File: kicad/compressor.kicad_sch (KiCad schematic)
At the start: 24 parts, among them J6 Conn_01x06, U8 NE5532, U9 NE5532

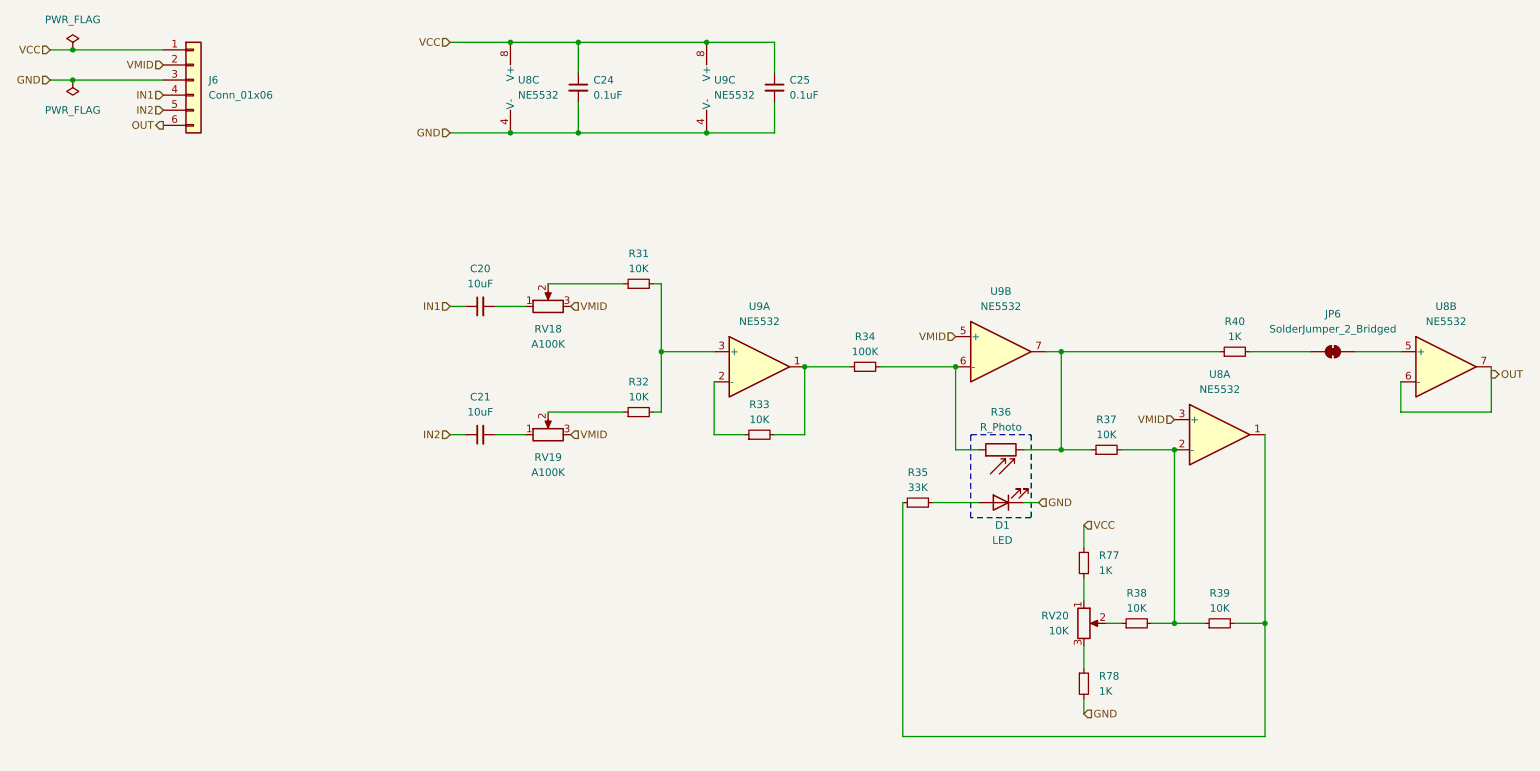
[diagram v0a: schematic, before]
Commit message: fix mixers in filter and compressor, update pcb
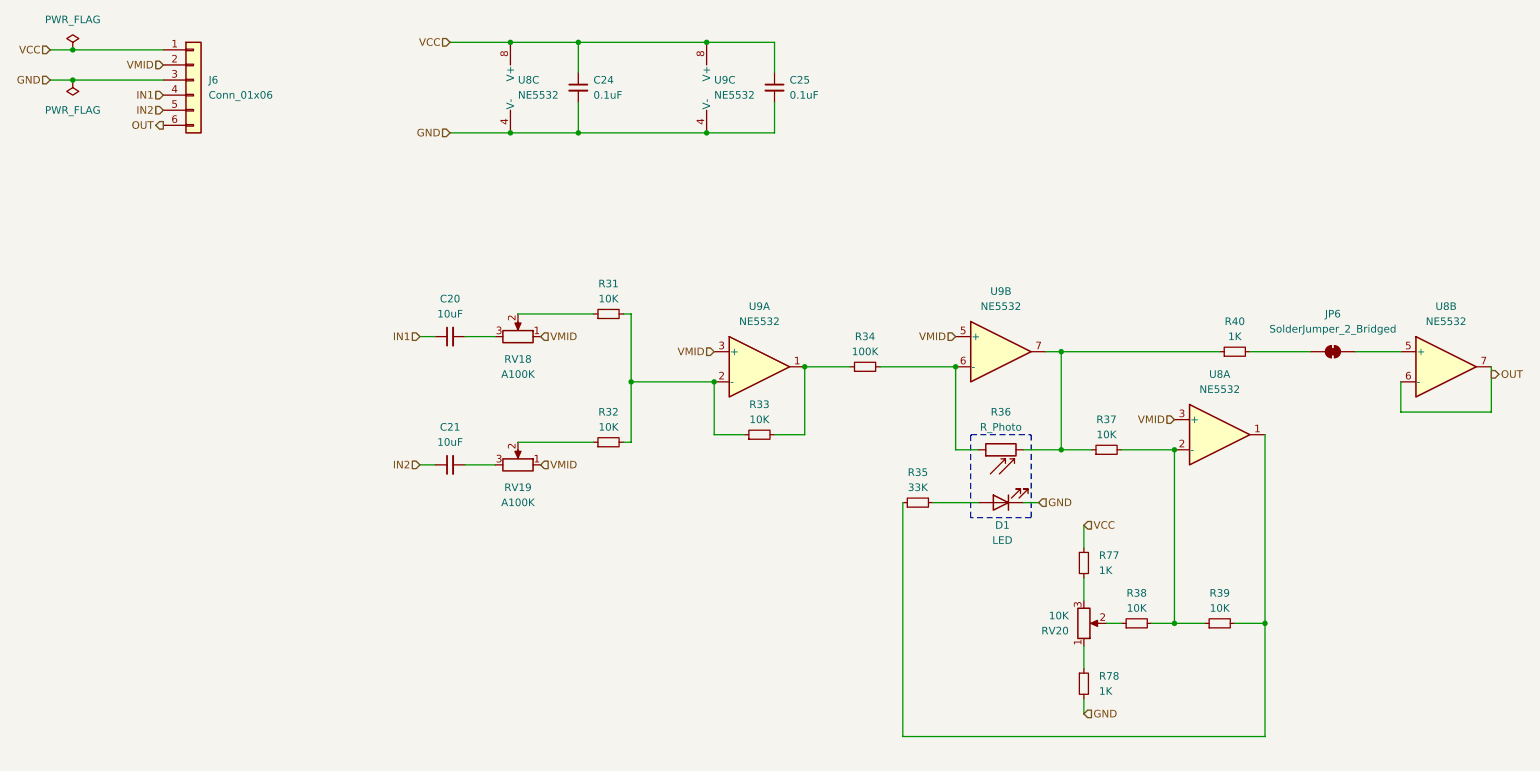
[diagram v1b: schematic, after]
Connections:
- net VMID: now also RV18.1, RV19.1, U9.3 (+); no longer RV18.3, RV19.3
- net at R33.1, U9.2 (-): now also R31.2, R32.2
- net at C21.2: now also RV19.3; no longer RV19.1
- net at R78.1: now also RV20.1; no longer RV20.3
- net at C20.2: now also RV18.3; no longer RV18.1
- net at R77.2: now also RV20.3; no longer RV20.1
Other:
- moved on the sheet: C20, C21, R31, R32, RV18, RV19
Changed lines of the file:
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@@
 	)
 	(junction
-		(at 125.73 88.9)
+		(at 120.65 93.98)
 		(diameter 0)
 		(color 0 0 0 0)
@@
 	)
 	(junction
+		(at 134.62 93.98)
+		(diameter 0)
+		(color 0 0 0 0)
+	)
+	(junction
 		(at 175.26 91.44)
 		(diameter 0)
@@
 	(wire
 		(pts
+			(xy 120.65 93.98) (xy 134.62 93.98)
+		)
+		(stroke
+			(width 0)
+			(type default)
+		)
+	)
+	(wire
+		(pts
 			(xy 111.76 52.07) (xy 133.35 52.07)
 		)
@@
 	(wire
 		(pts
-			(xy 106.68 77.47) (xy 119.38 77.47)
+			(xy 101.6 82.55) (xy 114.3 82.55)
 		)
 		(stroke
@@
 	(wire
 		(pts
-			(xy 97.79 102.87) (xy 102.87 102.87)
-		)
-		(stroke
-			(width 0)
-			(type default)
-		)
-	)
-	(wire
-		(pts
-			(xy 97.79 81.28) (xy 102.87 81.28)
+			(xy 92.71 107.95) (xy 97.79 107.95)
+		)
+		(stroke
+			(width 0)
+			(type default)
+		)
+	)
+	(wire
+		(pts
+			(xy 92.71 86.36) (xy 97.79 86.36)
 		)
 		(stroke
@@
 	(wire
 		(pts
-			(xy 125.73 77.47) (xy 125.73 88.9)
+			(xy 120.65 82.55) (xy 120.65 93.98)
 		)
 		(stroke
@@
 	(wire
 		(pts
+			(xy 120.65 93.98) (xy 120.65 104.14)
+		)
+		(stroke
+			(width 0)
+			(type default)
+		)
+	)
+	(wire
+		(pts
 			(xy 203.2 105.41) (xy 212.09 105.41)
 		)
@@
 	(wire
 		(pts
-			(xy 92.71 102.87) (xy 90.17 102.87)
-		)
-		(stroke
-			(width 0)
-			(type default)
-		)
-	)
-	(wire
-		(pts
-			(xy 125.73 88.9) (xy 125.73 99.06)
+			(xy 87.63 107.95) (xy 85.09 107.95)
 		)
 		(stroke
@@
 	(wire
 		(pts
-			(xy 92.71 81.28) (xy 90.17 81.28)
-		)
-		(stroke
-			(width 0)
-			(type default)
-		)
-	)
-	(wire
-		(pts
-			(xy 125.73 88.9) (xy 134.62 88.9)
+			(xy 87.63 86.36) (xy 85.09 86.36)
 		)
 		(stroke
@@
 	(wire
 		(pts
-			(xy 124.46 77.47) (xy 125.73 77.47)
+			(xy 119.38 82.55) (xy 120.65 82.55)
 		)
 		(stroke
@@
 	(wire
 		(pts
-			(xy 106.68 99.06) (xy 119.38 99.06)
+			(xy 101.6 104.14) (xy 114.3 104.14)
 		)
 		(stroke
@@
 	(wire
 		(pts
-			(xy 124.46 99.06) (xy 125.73 99.06)
+			(xy 119.38 104.14) (xy 120.65 104.14)
 		)
 		(stroke
@@
 		)
 	)
+	(hierarchical_label "VMID"
+		(shape input)
+		(at 134.62 88.9 180)
+		(effects
+			(font
+				(size 1.27 1.27)
+			)
+			(justify right)
+		)
+	)
 	(hierarchical_label "VCC"
 		(shape input)
@@
 	(hierarchical_label "VMID"
 		(shape input)
-		(at 110.49 81.28 0)
+		(at 105.41 86.36 0)
 		(effects
 			(font
@@
 	(hierarchical_label "VMID"
 		(shape input)
-		(at 110.49 102.87 0)
+		(at 105.41 107.95 0)
 		(effects
 			(font
@@
 	(hierarchical_label "IN2"
 		(shape input)
-		(at 90.17 102.87 180)
+		(at 85.09 107.95 180)
 		(effects
 			(font
@@
 	(hierarchical_label "IN1"
 		(shape input)
-		(at 90.17 81.28 180)
+		(at 85.09 86.36 180)
 		(effects
 			(font
@@
 		(on_board yes)
 		(dnp no)
-		(fields_autoplaced yes)
 		(property "Reference" "U9"
 			(at 142.24 81.28 0)
@@
 	(symbol
 		(lib_id "Device:R_Potentiometer")
-		(at 106.68 102.87 90)
+		(at 101.6 107.95 270)
+		(mirror x)
 		(unit 1)
 		(exclude_from_sim no)
@@
 		(on_board yes)
 		(dnp no)
-		(fields_autoplaced yes)
 		(property "Reference" "RV19"
-			(at 106.68 106.68 90)
+			(at 101.6 111.76 90)
 			(effects
 				(font
@@
 		)
 		(property "Value" "A100K"
-			(at 106.68 109.22 90)
+			(at 101.6 114.3 90)
 			(effects
 				(font
@@
 		)
 		(property "Footprint" "Pot_RV09AF-ALPHA:Pot_RV09AF-ALPHA"
-			(at 106.68 102.87 0)
+			(at 101.6 107.95 0)
 			(effects
 				(font
@@
 		)
 		(property "Datasheet" "~"
-			(at 106.68 102.87 0)
+			(at 101.6 107.95 0)
 			(effects
 				(font
@@
 		)
 		(property "Description" "Potentiometer"
-			(at 106.68 102.87 0)
+			(at 101.6 107.95 0)
 			(effects
 				(font
@@
 	(symbol
 		(lib_id "Device:R_Small")
-		(at 121.92 99.06 90)
+		(at 116.84 104.14 90)
 		(unit 1)
 		(exclude_from_sim no)
@@
 		(fields_autoplaced yes)
 		(property "Reference" "R32"
-			(at 121.92 93.98 90)
+			(at 116.84 99.06 90)
 			(effects
 				(font
@@
 		)
 		(property "Value" "10K"
-			(at 121.92 96.52 90)
+			(at 116.84 101.6 90)
 			(effects
 				(font
@@
 		)
 		(property "Footprint" "Resistor_SMD:R_0603_1608Metric"
-			(at 121.92 99.06 0)
+			(at 116.84 104.14 0)
 			(effects
 				(font
@@
 		)
 		(property "Datasheet" "~"
-			(at 121.92 99.06 0)
+			(at 116.84 104.14 0)
 			(effects
 				(font
@@
 		)
 		(property "Description" "Resistor, small symbol"
-			(at 121.92 99.06 0)
+			(at 116.84 104.14 0)
 			(effects
 				(font
@@
 	(symbol
 		(lib_id "Device:C_Small")
-		(at 95.25 81.28 90)
+		(at 90.17 86.36 90)
 		(unit 1)
 		(exclude_from_sim no)
@@
 		(fields_autoplaced yes)
 		(property "Reference" "C20"
-			(at 95.2563 74.93 90)
+			(at 90.1763 80.01 90)
 			(effects
 				(font
@@
 		)
 		(property "Value" "10uF"
-			(at 95.2563 77.47 90)
+			(at 90.1763 82.55 90)
 			(effects
 				(font
@@
 		)
 		(property "Footprint" "Capacitor_SMD:C_0805_2012Metric"
-			(at 95.25 81.28 0)
+			(at 90.17 86.36 0)
 			(effects
 				(font
@@
 		)
 		(property "Datasheet" "~"
-			(at 95.25 81.28 0)
+			(at 90.17 86.36 0)
 			(effects
 				(font
@@
 		)
 		(property "Description" "Unpolarized capacitor, small symbol"
-			(at 95.25 81.28 0)
+			(at 90.17 86.36 0)
 			(effects
 				(font
@@
 		(lib_id "Device:R_Potentiometer")
 		(at 196.85 134.62 0)
+		(mirror x)
 		(unit 1)
 		(exclude_from_sim no)
@@
 		(on_board yes)
 		(dnp no)
-		(fields_autoplaced yes)
 		(property "Reference" "RV20"
-			(at 194.31 133.3499 0)
+			(at 194.31 135.8901 0)
 			(effects
 				(font
@@
 		)
 		(property "Value" "10K"
-			(at 194.31 135.8899 0)
+			(at 194.31 133.3501 0)
 			(effects
 				(font
@@
 	(symbol
 		(lib_id "Device:R_Small")
-		(at 121.92 77.47 90)
+		(at 116.84 82.55 90)
 		(unit 1)
 		(exclude_from_sim no)
@@
 		(fields_autoplaced yes)
 		(property "Reference" "R31"
-			(at 121.92 72.39 90)
+			(at 116.84 77.47 90)
 			(effects
 				(font
@@
 		)
 		(property "Value" "10K"
-			(at 121.92 74.93 90)
+			(at 116.84 80.01 90)
 			(effects
 				(font
@@
 		)
 		(property "Footprint" "Resistor_SMD:R_0603_1608Metric"
-			(at 121.92 77.47 0)
+			(at 116.84 82.55 0)
 			(effects
 				(font
@@
 		)
 		(property "Datasheet" "~"
-			(at 121.92 77.47 0)
+			(at 116.84 82.55 0)
 			(effects
 				(font
@@
 		)
 		(property "Description" "Resistor, small symbol"
-			(at 121.92 77.47 0)
+			(at 116.84 82.55 0)
 			(effects
 				(font
@@
 	(symbol
 		(lib_id "Device:R_Potentiometer")
-		(at 106.68 81.28 90)
+		(at 101.6 86.36 270)
+		(mirror x)
 		(unit 1)
 		(exclude_from_sim no)
@@
 		(on_board yes)
 		(dnp no)
-		(fields_autoplaced yes)
 		(property "Reference" "RV18"
-			(at 106.68 85.09 90)
+			(at 101.6 90.17 90)
 			(effects
 				(font
@@
 		)
 		(property "Value" "A100K"
-			(at 106.68 87.63 90)
+			(at 101.6 92.71 90)
 			(effects
 				(font
@@
 		)
 		(property "Footprint" "Pot_RV09AF-ALPHA:Pot_RV09AF-ALPHA"
-			(at 106.68 81.28 0)
+			(at 101.6 86.36 0)
 			(effects
 				(font
@@
 		)
 		(property "Datasheet" "~"
-			(at 106.68 81.28 0)
+			(at 101.6 86.36 0)
 			(effects
 				(font
@@
 		)
 		(property "Description" "Potentiometer"
-			(at 106.68 81.28 0)
+			(at 101.6 86.36 0)
 			(effects
 				(font
@@
 	(symbol
 		(lib_id "Device:C_Small")
-		(at 95.25 102.87 90)
+		(at 90.17 107.95 90)
 		(unit 1)
 		(exclude_from_sim no)
@@
 		(fields_autoplaced yes)
 		(property "Reference" "C21"
-			(at 95.2563 96.52 90)
+			(at 90.1763 101.6 90)
 			(effects
 				(font
@@
 		)
 		(property "Value" "10uF"
-			(at 95.2563 99.06 90)
+			(at 90.1763 104.14 90)
 			(effects
 				(font
@@
 		)
 		(property "Footprint" "Capacitor_SMD:C_0805_2012Metric"
-			(at 95.25 102.87 0)
+			(at 90.17 107.95 0)
 			(effects
 				(font
@@
 		)
 		(property "Datasheet" "~"
-			(at 95.25 102.87 0)
+			(at 90.17 107.95 0)
 			(effects
 				(font
@@
 		)
 		(property "Description" "Unpolarized capacitor, small symbol"
-			(at 95.25 102.87 0)
-			(effects
-				(font
+			(at 90.17 107.95 0)
+			(effects
+				(font

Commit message: mark components as DNP, add LCSC part numbers
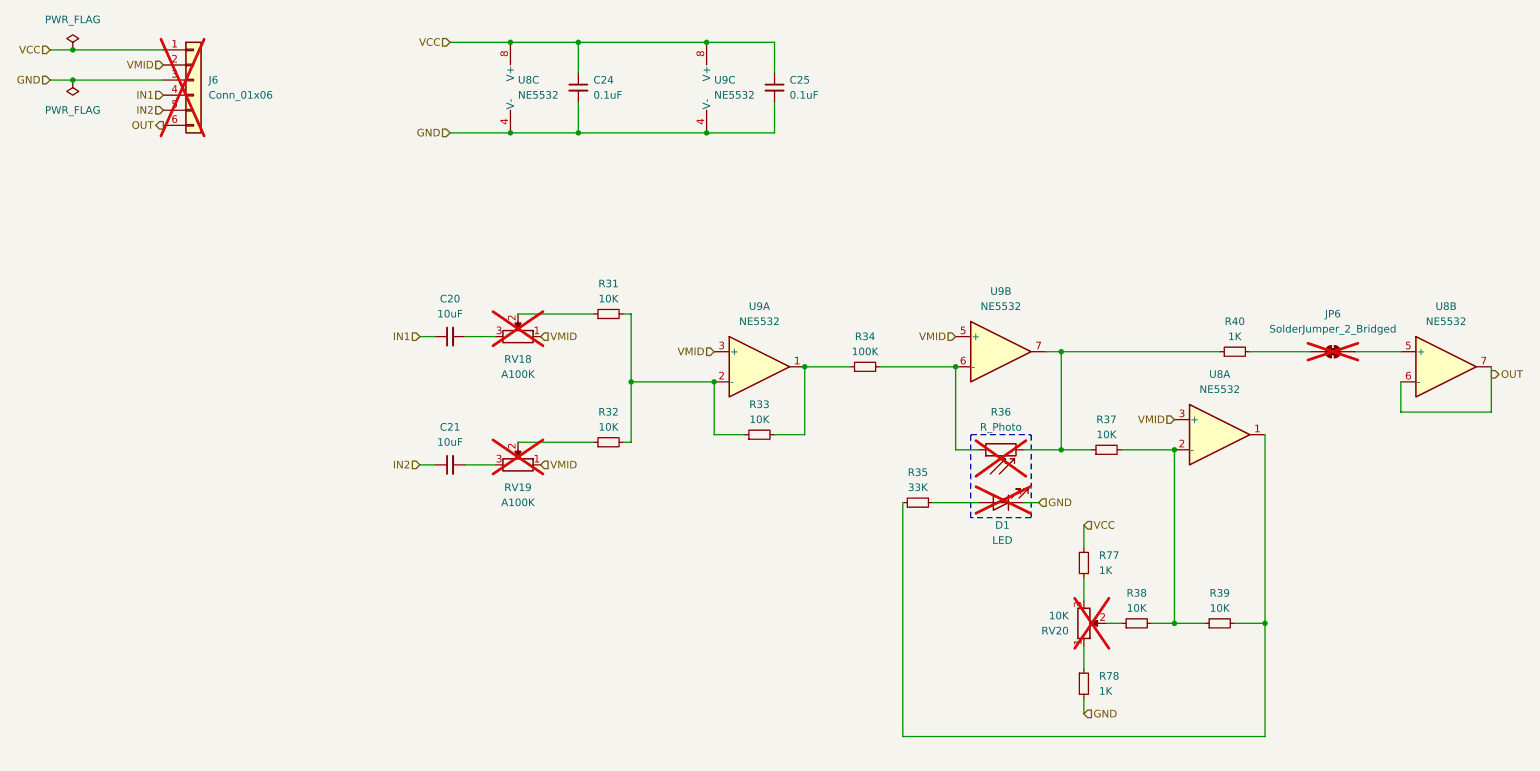
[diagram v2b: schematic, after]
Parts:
- D1, J6, JP6, R36, RV18, RV19, RV20: now not fitted
- U8, U9: JLC (none) -> C7426

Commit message: add local changes
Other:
- moved on the sheet: C20, C21, D1, JP6, R31, R32, R33, R34, R35, R36, R37, R38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
